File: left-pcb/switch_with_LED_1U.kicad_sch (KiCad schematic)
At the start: 3 parts, among them SW1 SW_SPST

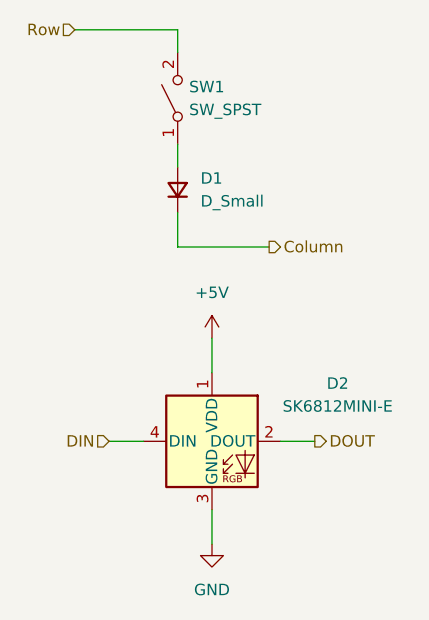
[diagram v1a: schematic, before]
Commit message: Initial modifications to reduce fab cost and add caps
Removing 1 row and column of keys, and majorly changing layout

Routing still in progress
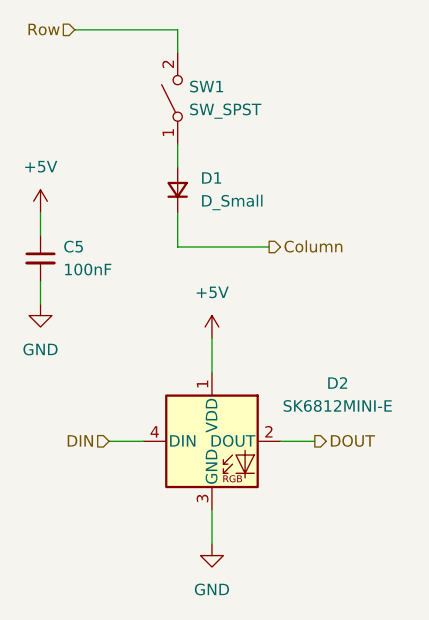
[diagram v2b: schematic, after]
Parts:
- added C5: 100nF, Capacitor_SMD:C_1206_3216Metric_Pad1.33x1.80mm_HandSolder, symbol Device:C_Small
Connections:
- net +5V: now also C5.1
- net GND: now also C5.2

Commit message: Caps, shrunk board, added mounting holes
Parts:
- C5: footprint Capacitor_SMD:C_1206_3216Metric_Pad1.33x1.80mm_HandSolder -> Capacitor_SMD:C_0805_2012Metric_Pad1.18x1.45mm_HandSolder
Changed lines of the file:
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@@
 			)
 		)
-		(property "Footprint" "Capacitor_SMD:C_1206_3216Metric_Pad1.33x1.80mm_HandSolder"
+		(property "Footprint" "Capacitor_SMD:C_0805_2012Metric_Pad1.18x1.45mm_HandSolder"
 			(at 105.41 111.76 0)
 			(effects

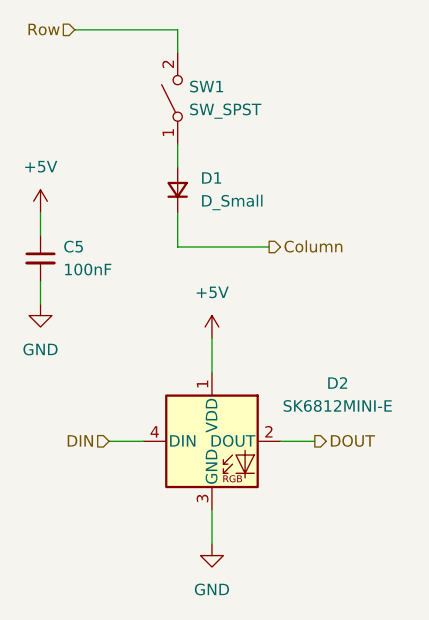
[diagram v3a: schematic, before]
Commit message: Adding values to Diodes and adding stabilizers to 2U switches
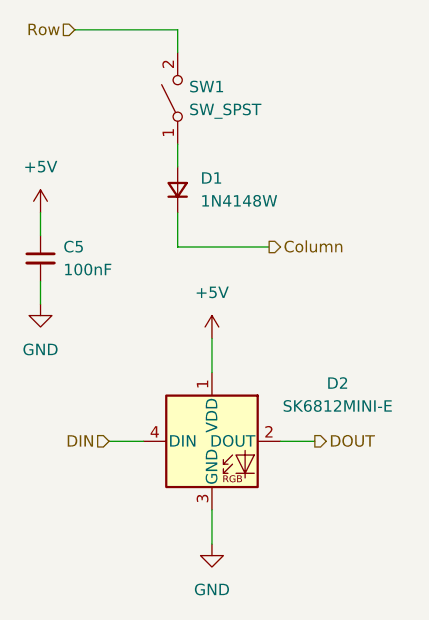
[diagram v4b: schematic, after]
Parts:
- D1: value D_Small -> 1N4148W
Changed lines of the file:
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@@
 			)
 		)
-		(property "Value" "D_Small"
+		(property "Value" "1N4148W"
 			(at 123.19 105.4099 90)
 			(effects

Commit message: Added extra column to left hand keyboard
Matching size to right hand side.
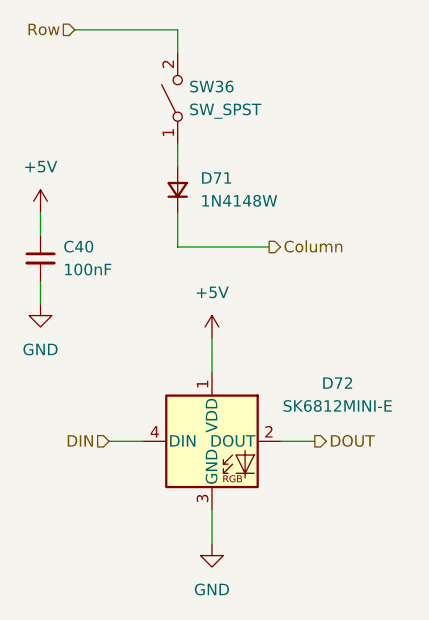
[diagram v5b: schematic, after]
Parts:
- renumbered C5 to C40, D1 to D71, D2 to D72, SW1 to SW36

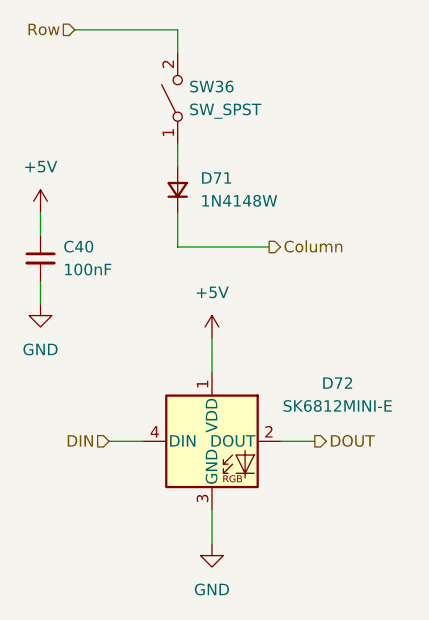
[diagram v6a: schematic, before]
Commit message: adding mounting hole in center for additional support, and cleaning up tracks/zones
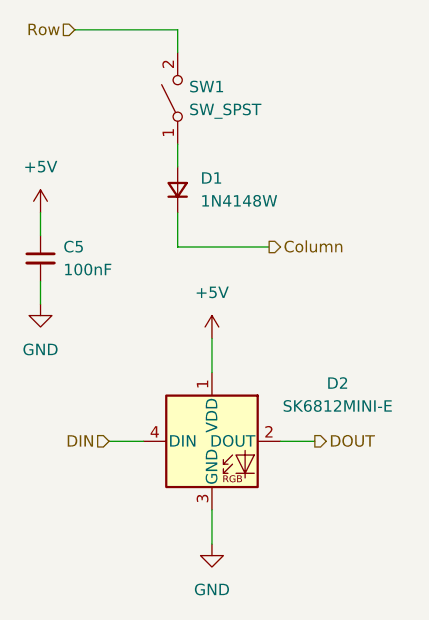
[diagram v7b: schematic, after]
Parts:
- renumbered C40 to C5, D71 to D1, D72 to D2, SW36 to SW1

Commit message: Boards were ordered
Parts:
- SW1: symbol Switch:SW_SPST -> SW-gElectroMech:SPST_MOM
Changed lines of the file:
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@@
 	)
 	(symbol
-		(lib_id "Switch:SW_SPST")
+		(lib_id "SW-gElectroMech:SPST_MOM")
 		(at 120.65 93.98 90)
 		(unit 1)
@@
 		)
 		(property "Datasheet" ""
-			(at 120.65 93.98 0)
+			(at 115.57 93.98 0)
 			(hide yes)
 			(show_name no)
@@
 			)
 		)
-		(property "Description" "Single Pole Single Throw (SPST) switch"
+		(property "Description" "Push button switch, generic, two pins"
 			(at 120.65 93.98 0)
 			(hide yes)
